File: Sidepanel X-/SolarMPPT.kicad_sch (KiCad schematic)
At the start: 19 parts

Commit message: Diode D1 angebracht
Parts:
- added D1: PMEG2020EH, Diode_SMD:D_SOD-123F, symbol Diode:PMEG2020EH
- L_IN1: value (none) -> 10u; footprint (none) -> STS_Inductor_SMD:XAL6060103MEC
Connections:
- net MPPT1_IN: now also D1.2 (A)
- net MPPT1_OUT: now also D1.1 (K)
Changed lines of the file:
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@@
   (junction (at 148.59 57.15) (diameter 0) (color 0 0 0 0)
   )
+  (junction (at 144.78 46.99) (diameter 0) (color 0 0 0 0)
+  )
   (junction (at 58.42 46.99) (diameter 0) (color 0 0 0 0)
   )
@@
   (junction (at 81.28 46.99) (diameter 0) (color 0 0 0 0)
   )
+  (junction (at 104.14 31.75) (diameter 0) (color 0 0 0 0)
+  )
   (junction (at 95.25 54.61) (diameter 0) (color 0 0 0 0)
   )
@@
     (stroke (width 0) (type default) (color 0 0 0 0))
   )
-  (wire (pts (xy 104.14 39.37) (xy 104.14 46.99))
-    (stroke (width 0) (type default) (color 0 0 0 0))
-  )
   (wire (pts (xy 148.59 57.15) (xy 148.59 54.61))
     (stroke (width 0) (type default) (color 0 0 0 0))
@@
     (stroke (width 0) (type default) (color 0 0 0 0))
   )
+  (wire (pts (xy 104.14 31.75) (xy 120.65 31.75))
+    (stroke (width 0) (type default) (color 0 0 0 0))
+  )
   (wire (pts (xy 144.78 52.07) (xy 149.86 52.07))
     (stroke (width 0) (type default) (color 0 0 0 0))
@@
     (stroke (width 0) (type default) (color 0 0 0 0))
   )
+  (wire (pts (xy 104.14 26.67) (xy 104.14 31.75))
+    (stroke (width 0) (type default) (color 0 0 0 0))
+  )
   (wire (pts (xy 60.96 46.99) (xy 60.96 48.26))
     (stroke (width 0) (type default) (color 0 0 0 0))
@@
     (stroke (width 0) (type default) (color 0 0 0 0))
   )
+  (wire (pts (xy 144.78 31.75) (xy 144.78 46.99))
+    (stroke (width 0) (type default) (color 0 0 0 0))
+  )
   (wire (pts (xy 176.53 57.15) (xy 148.59 57.15))
     (stroke (width 0) (type default) (color 0 0 0 0))
@@
     (stroke (width 0) (type default) (color 0 0 0 0))
   )
+  (wire (pts (xy 104.14 31.75) (xy 104.14 46.99))
+    (stroke (width 0) (type default) (color 0 0 0 0))
+  )
   (wire (pts (xy 148.59 64.77) (xy 148.59 63.5))
     (stroke (width 0) (type default) (color 0 0 0 0))
@@
   )
   (wire (pts (xy 144.78 46.99) (xy 146.05 46.99))
+    (stroke (width 0) (type default) (color 0 0 0 0))
+  )
+  (wire (pts (xy 128.27 31.75) (xy 144.78 31.75))
     (stroke (width 0) (type default) (color 0 0 0 0))
   )
@@
   (hierarchical_label "MPPT1" (shape output) (at 195.58 43.18 0)
     (effects (font (size 1.27 1.27)) (justify left))
+  )
+  (symbol (lib_id "Diode:PMEG2020EH") (at 124.46 31.75 0) (mirror y) (unit 1)
+    (in_bom yes) (on_board yes) (fields_autoplaced)
+    (property "Reference" "D1" (id 0) (at 124.7775 25.4 0))
+    (property "Value" "PMEG2020EH" (id 1) (at 124.7775 27.94 0))
+    (property "Footprint" "Diode_SMD:D_SOD-123F" (id 2) (at 124.46 36.195 0)
+      (effects (font (size 1.27 1.27)) hide)
+    )
+    (property "Datasheet" "https://assets.nexperia.com/documents/data-sheet/PMEG2020EH_EJ.pdf" (id 3) (at 124.46 31.75 0)
+      (effects (font (size 1.27 1.27)) hide)
+    )
+    (pin "1")
+    (pin "2")
   )
   (symbol (lib_id "Device:R_Small") (at 170.18 43.18 270) (unit 1)
@@
     (in_bom yes) (on_board yes) (fields_autoplaced)
     (property "Reference" "L_IN1" (id 0) (at 100.33 41.91 90))
-    (property "Value" "" (id 1) (at 100.33 44.45 90))
-    (property "Footprint" "" (id 2) (at 100.33 46.99 0)
-      (effects (font (size 1.27 1.27)) hide)
-    )
+    (property "Value" "10u" (id 1) (at 100.33 44.45 90))
+    (property "Footprint" "STS_Inductor_SMD:XAL6060103MEC" (id 2) (at 100.33 46.99 0)
+      (effects (font (size 1.27 1.27)) hide)
+    )

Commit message: small adjustments
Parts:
- L_IN1: footprint STS_Inductor_SMD:XAL6060103MEC -> STS_Inductor_SMD:IND_XAL6060-103MEC
- R21: value tbd -> 330k
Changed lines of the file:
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@@
   (junction (at 153.67 46.99) (diameter 0) (color 0 0 0 0)
   )
+  (junction (at 104.14 33.02) (diameter 0) (color 0 0 0 0)
+  )
   (junction (at 58.42 81.28) (diameter 0) (color 0 0 0 0)
   )
@@
   (junction (at 148.59 57.15) (diameter 0) (color 0 0 0 0)
   )
-  (junction (at 144.78 46.99) (diameter 0) (color 0 0 0 0)
-  )
   (junction (at 58.42 46.99) (diameter 0) (color 0 0 0 0)
   )
@@
   (junction (at 39.37 46.99) (diameter 0) (color 0 0 0 0)
   )
+  (junction (at 146.05 43.18) (diameter 0) (color 0 0 0 0)
+  )
   (junction (at 95.25 46.99) (diameter 0) (color 0 0 0 0)
   )
@@
   (junction (at 81.28 46.99) (diameter 0) (color 0 0 0 0)
   )
-  (junction (at 104.14 31.75) (diameter 0) (color 0 0 0 0)
-  )
   (junction (at 95.25 54.61) (diameter 0) (color 0 0 0 0)
   )
@@
     (stroke (width 0) (type default) (color 0 0 0 0))
   )
+  (wire (pts (xy 104.14 27.94) (xy 104.14 33.02))
+    (stroke (width 0) (type default) (color 0 0 0 0))
+  )
+  (wire (pts (xy 146.05 33.02) (xy 146.05 43.18))
+    (stroke (width 0) (type default) (color 0 0 0 0))
+  )
   (wire (pts (xy 148.59 57.15) (xy 148.59 54.61))
     (stroke (width 0) (type default) (color 0 0 0 0))
@@
     (stroke (width 0) (type default) (color 0 0 0 0))
   )
-  (wire (pts (xy 104.14 31.75) (xy 120.65 31.75))
-    (stroke (width 0) (type default) (color 0 0 0 0))
-  )
   (wire (pts (xy 144.78 52.07) (xy 149.86 52.07))
     (stroke (width 0) (type default) (color 0 0 0 0))
@@
     (stroke (width 0) (type default) (color 0 0 0 0))
   )
-  (wire (pts (xy 104.14 26.67) (xy 104.14 31.75))
-    (stroke (width 0) (type default) (color 0 0 0 0))
-  )
   (wire (pts (xy 60.96 46.99) (xy 60.96 48.26))
     (stroke (width 0) (type default) (color 0 0 0 0))
@@
     (stroke (width 0) (type default) (color 0 0 0 0))
   )
+  (wire (pts (xy 104.14 33.02) (xy 104.14 46.99))
+    (stroke (width 0) (type default) (color 0 0 0 0))
+  )
   (wire (pts (xy 190.5 57.15) (xy 190.5 64.77))
     (stroke (width 0) (type default) (color 0 0 0 0))
@@
     (stroke (width 0) (type default) (color 0 0 0 0))
   )
-  (wire (pts (xy 144.78 31.75) (xy 144.78 46.99))
-    (stroke (width 0) (type default) (color 0 0 0 0))
-  )
   (wire (pts (xy 176.53 57.15) (xy 148.59 57.15))
     (stroke (width 0) (type default) (color 0 0 0 0))
@@
     (stroke (width 0) (type default) (color 0 0 0 0))
   )
-  (wire (pts (xy 104.14 31.75) (xy 104.14 46.99))
-    (stroke (width 0) (type default) (color 0 0 0 0))
-  )
   (wire (pts (xy 148.59 64.77) (xy 148.59 63.5))
     (stroke (width 0) (type default) (color 0 0 0 0))
@@
     (stroke (width 0) (type default) (color 0 0 0 0))
   )
-  (wire (pts (xy 128.27 31.75) (xy 144.78 31.75))
+  (wire (pts (xy 104.14 33.02) (xy 120.65 33.02))
     (stroke (width 0) (type default) (color 0 0 0 0))
   )
   (wire (pts (xy 166.37 46.99) (xy 165.1 46.99))
+    (stroke (width 0) (type default) (color 0 0 0 0))
+  )
+  (wire (pts (xy 128.27 33.02) (xy 146.05 33.02))
     (stroke (width 0) (type default) (color 0 0 0 0))
   )
@@
   (hierarchical_label "MPPT1" (shape output) (at 195.58 43.18 0)
     (effects (font (size 1.27 1.27)) (justify left))
-  )
-  (symbol (lib_id "Diode:PMEG2020EH") (at 124.46 31.75 0) (mirror y) (unit 1)
-    (in_bom yes) (on_board yes) (fields_autoplaced)
-    (property "Reference" "D1" (id 0) (at 124.7775 25.4 0))
-    (property "Value" "PMEG2020EH" (id 1) (at 124.7775 27.94 0))
-    (property "Footprint" "Diode_SMD:D_SOD-123F" (id 2) (at 124.46 36.195 0)
-      (effects (font (size 1.27 1.27)) hide)
-    )
-    (property "Datasheet" "https://assets.nexperia.com/documents/data-sheet/PMEG2020EH_EJ.pdf" (id 3) (at 124.46 31.75 0)
-      (effects (font (size 1.27 1.27)) hide)
-    )
-    (pin "1")
-    (pin "2")
   )
   (symbol (lib_id "Device:R_Small") (at 170.18 43.18 270) (unit 1)
@@
       (effects (font (size 1.27 1.27)) (justify right))
     )
-    (property "Value" "tbd" (id 1) (at 179.07 62.2299 0)
+    (property "Value" "330k" (id 1) (at 179.07 62.2299 0)
       (effects (font (size 1.27 1.27)) (justify right))
     )
@@
     (property "Reference" "L_IN1" (id 0) (at 100.33 41.91 90))
     (property "Value" "10u" (id 1) (at 100.33 44.45 90))
-    (property "Footprint" "STS_Inductor_SMD:XAL6060103MEC" (id 2) (at 100.33 46.99 0)
+    (property "Footprint" "STS_Inductor_SMD:IND_XAL6060-103MEC" (id 2) (at 100.33 46.99 0)
       (effects (font (size 1.27 1.27)) hide)
     )
@@
       (effects (font (size 1.27 1.27)) hide)
     )
+    (pin "1")
+    (pin "2")
+  )
+  (symbol (lib_id "Diode:PMEG2020EH") (at 124.46 33.02 0) (mirror y) (unit 1)
+    (in_bom yes) (on_board yes) (fields_autoplaced)
+    (property "Reference" "D1" (id 0) (at 124.7775 26.67 0))
+    (property "Value" "PMEG2020EH" (id 1) (at 124.7775 29.21 0))
+    (property "Footprint" "Diode_SMD:D_SOD-123F" (id 2) (at 124.46 37.465 0)
+      (effects (font (size 1.27 1.27)) hide)
+    )
+    (property "Datasheet" "https://assets.nexperia.com/documents/data-sheet/PMEG2020EH_EJ.pdf" (id 3) (at 124.46 33.02 0)
+      (effects (font (size 1.27 1.27)) hide)
+    )

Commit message: small adjustments
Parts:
- SC1: footprint STS_Solarcells:3G30A_40x80 -> STS_solder:3G30A_40x80
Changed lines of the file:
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@@
       (effects (font (size 1.27 1.27)) (justify left))
     )
-    (property "Footprint" "STS_Solarcells:3G30A_40x80" (id 2) (at 39.37 51.816 90)
+    (property "Footprint" "STS_solder:3G30A_40x80" (id 2) (at 39.37 51.816 90)
       (effects (font (size 1.27 1.27)) hide)
     )

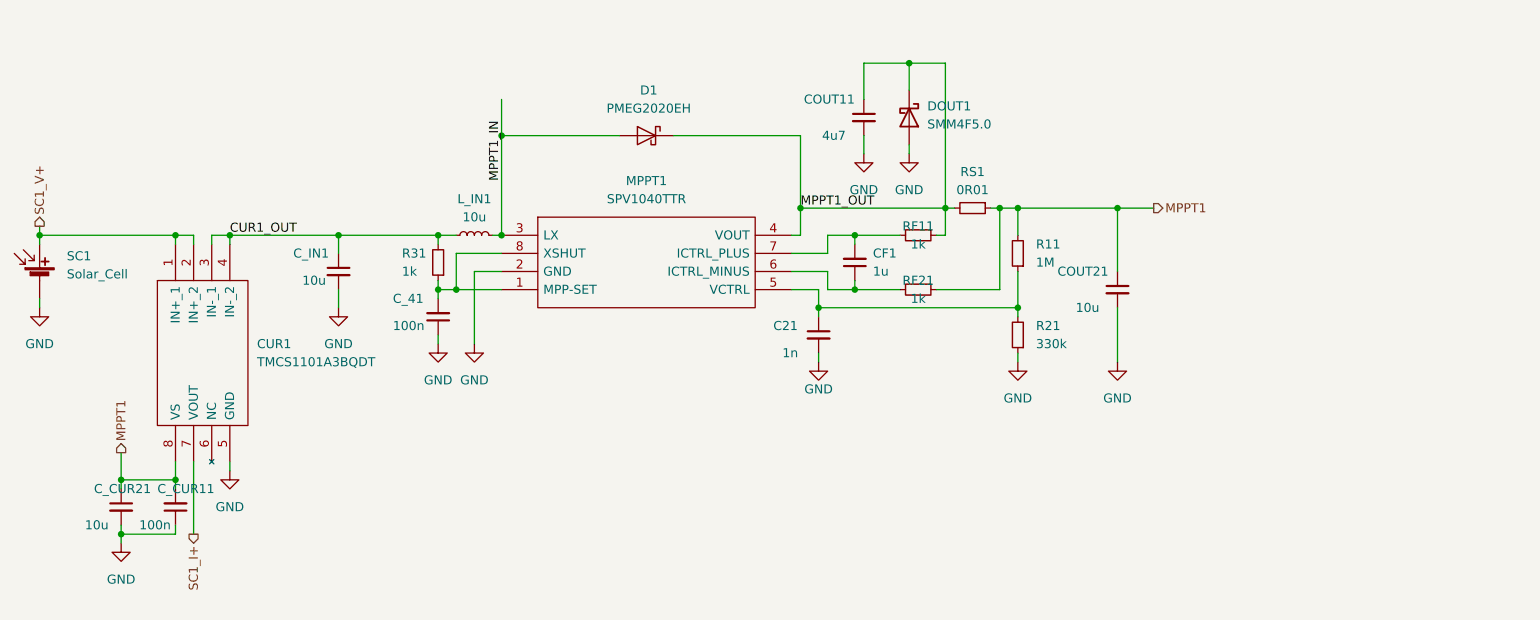
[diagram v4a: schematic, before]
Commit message: changes to the solar cell footprint + added alternative current sensing solution
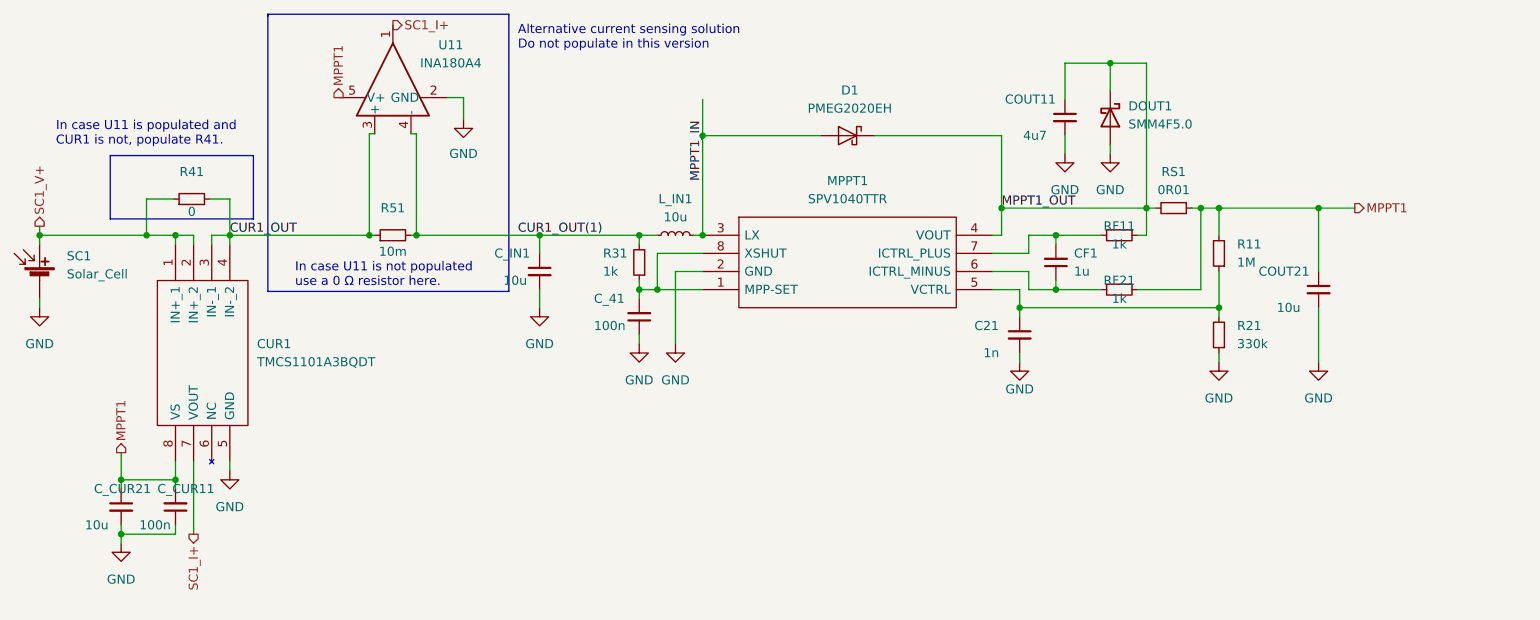
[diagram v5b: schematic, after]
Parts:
- added R41: 0, Resistor_SMD:R_0603_1608Metric, symbol Device:R_Small
- added R51: 10m, Resistor_SMD:R_0603_1608Metric, symbol Device:R_Small
- added U11: INA180A4, Package_TO_SOT_SMD:SOT-23-5, symbol Amplifier_Current:INA180A4
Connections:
- net CUR1_OUT: now also R41.2, R51.1, U11.3 (+); no longer C_IN1.1, L_IN1.1, R31.2
- net GND: now also U11.2 (GND)
- net MPPT1: now also U11.5 (V+)
- net SC1_I+: now also U11.1
- net SC1_V+: now also R41.1
- new net CUR1_OUT(1): C_IN1.1, L_IN1.1, R31.2, R51.2, U11.4 (-)
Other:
- note added: "Alternative current sensing solution Do not populate in this version"
- note added: "In case U11 is not populated use a 0 Ω resistor here."
- note added: "In case U11 is populated and CUR1 is not, populate R41."
- moved on the sheet: C21, CF1, COUT11, COUT21, C_41, C_IN1, D1, DOUT1, L_IN1, MPPT1, R11, R21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

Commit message: changed the x+ and x- axis
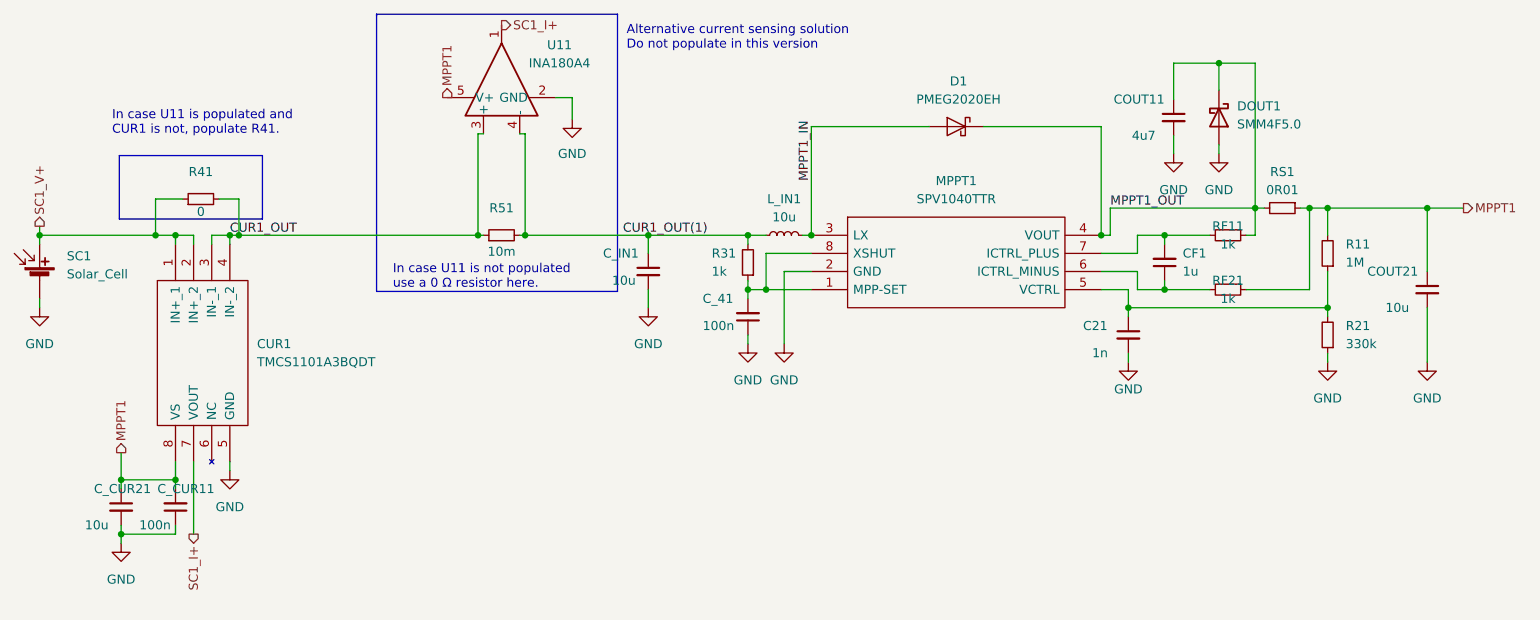
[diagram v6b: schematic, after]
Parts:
- L_IN1: footprint STS_Inductor_SMD:IND_XAL6060-103MEC -> STS_Inductor_SMD:XAL6060103MEC
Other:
- moved on the sheet: C21, CF1, COUT11, COUT21, C_41, C_IN1, DOUT1, L_IN1, MPPT1, R11, R21, R31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
